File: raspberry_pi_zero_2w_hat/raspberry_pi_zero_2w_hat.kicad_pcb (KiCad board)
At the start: 2 copper layers, 65 x 30 mm, 5 parts, among them J1 GPIO

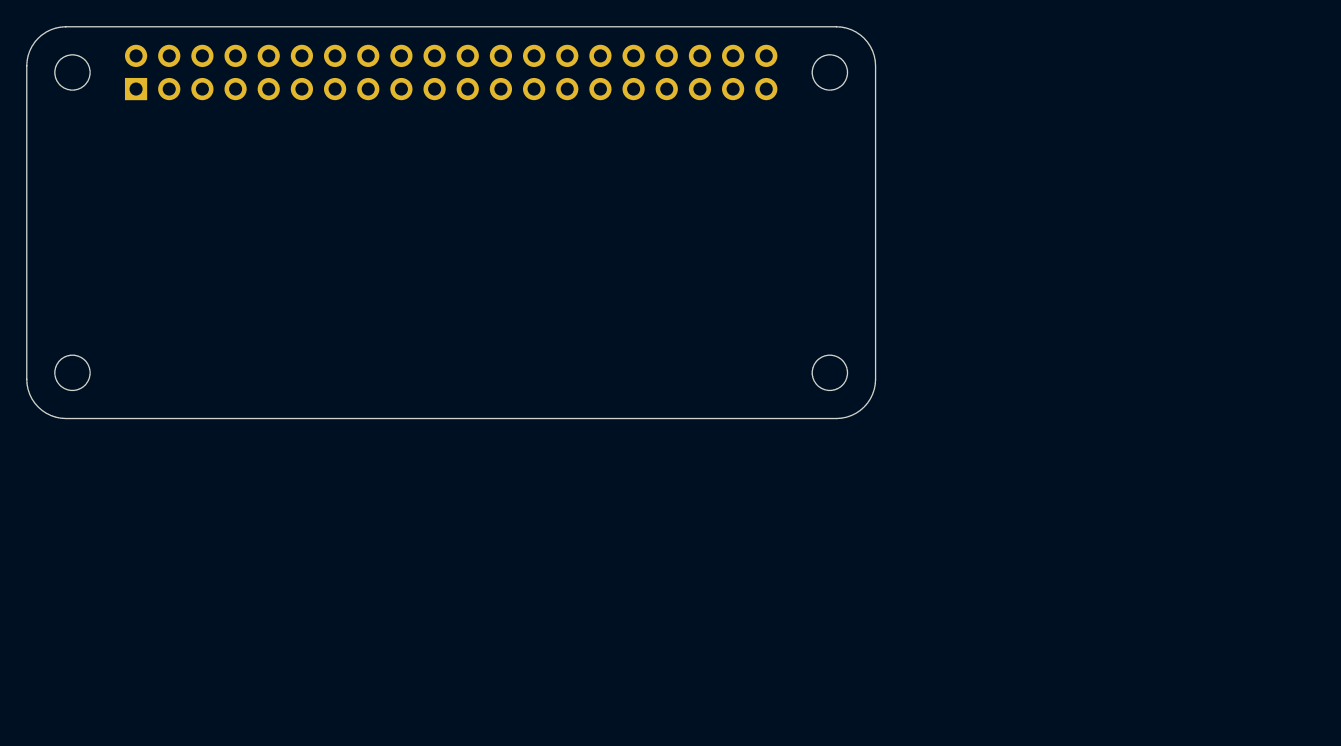
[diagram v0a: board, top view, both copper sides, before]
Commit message: Added symbols, footprints and first layout
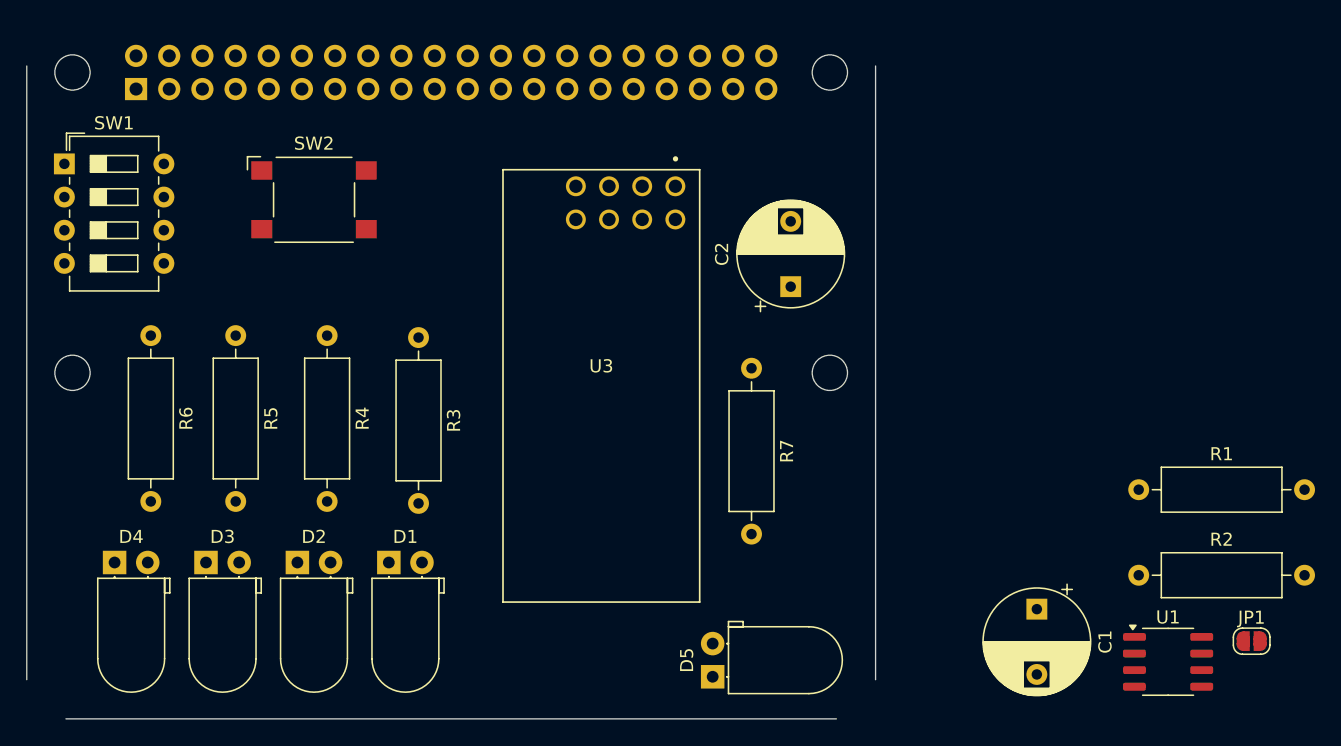
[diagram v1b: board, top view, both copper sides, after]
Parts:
- added C1: 100n, Capacitor_THT:CP_Radial_D8.0mm_P5.00mm, F.Cu at (177.3, 114.6)
- added C2: 47uF, Capacitor_THT:CP_Radial_D8.0mm_P5.00mm, F.Cu at (158.5, 89.9)
- added D1: LED, LED_THT:LED_D5.0mm_Horizontal_O1.27mm_Z3.0mm, F.Cu at (127.7, 111.0)
- added D2: LED, LED_THT:LED_D5.0mm_Horizontal_O1.27mm_Z3.0mm, F.Cu at (120.7, 111.0)
- added D3: LED, LED_THT:LED_D5.0mm_Horizontal_O1.27mm_Z3.0mm, F.Cu at (113.7, 111.0)
- added D4: LED, LED_THT:LED_D5.0mm_Horizontal_O1.27mm_Z3.0mm, F.Cu at (106.7, 111.0)
- added D5: LED, LED_THT:LED_D5.0mm_Horizontal_O1.27mm_Z3.0mm, F.Cu at (152.5, 119.8)
- added JP1: ID_WP, Jumper:SolderJumper-2_P1.3mm_Open_RoundedPad1.0x1.5mm, F.Cu at (193.8, 117.0)
- added R1: 3.9k, Resistor_THT:R_Axial_DIN0309_L9.0mm_D3.2mm_P12.70mm_Horizontal, F.Cu at (185.2, 105.5)
- added R2: 3.9k, Resistor_THT:R_Axial_DIN0309_L9.0mm_D3.2mm_P12.70mm_Horizontal, F.Cu at (185.2, 112.0)
- added R3: 220, Resistor_THT:R_Axial_DIN0309_L9.0mm_D3.2mm_P12.70mm_Horizontal, F.Cu at (130.0, 93.8)
- added R4: 220, Resistor_THT:R_Axial_DIN0309_L9.0mm_D3.2mm_P12.70mm_Horizontal, F.Cu at (123.0, 93.7)
- added R5: 220, Resistor_THT:R_Axial_DIN0309_L9.0mm_D3.2mm_P12.70mm_Horizontal, F.Cu at (116.0, 93.7)
- added R6: 220, Resistor_THT:R_Axial_DIN0309_L9.0mm_D3.2mm_P12.70mm_Horizontal, F.Cu at (109.5, 93.7)
- added R7: 220, Resistor_THT:R_Axial_DIN0309_L9.0mm_D3.2mm_P12.70mm_Horizontal, F.Cu at (155.5, 96.2)
- added SW1: SW_DIP_x04, Button_Switch_THT:SW_DIP_SPSTx04_Slide_6.7x11.72mm_W7.62mm_P2.54mm_LowProfile, F.Cu at (102.9, 80.5)
- added SW2: SW_Nidec_CAS-120A1, Button_Switch_SMD:SW_SPST_Omron_B3FS-101xP, F.Cu at (122.0, 83.2)
- added U1: CAT24C256, Package_SO:SO-8_3.9x4.9mm_P1.27mm, F.Cu at (187.4, 118.6)
- added U3: NRF24L01P, NRF24L01P-MODULE-PCB:XCVR_NRF24L01P-MODULE-PCB, F.Cu at (144.0, 97.5)
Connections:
- J1 pad 22: /GPIO25 -> CE
- J1 pad 24: /GPIO8/SPI0.CE0 -> CSN
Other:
- board size 65 x 30 mm -> 65 x 50 mm
- board text removed: "Extend PCB edge 0.5mm if using SMT header"
